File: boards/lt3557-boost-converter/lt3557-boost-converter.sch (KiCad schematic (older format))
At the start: 3 parts

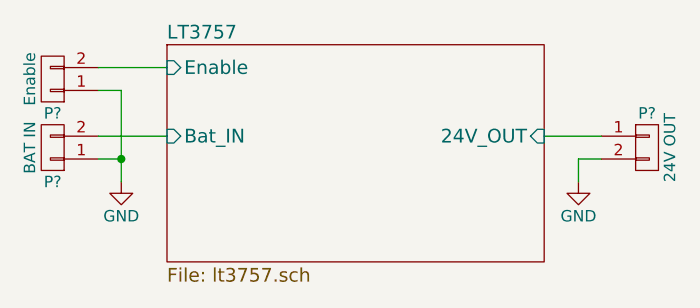
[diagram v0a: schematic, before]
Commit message: lt3557-boost-converter: schematic finished; parts selected; footprints assigned
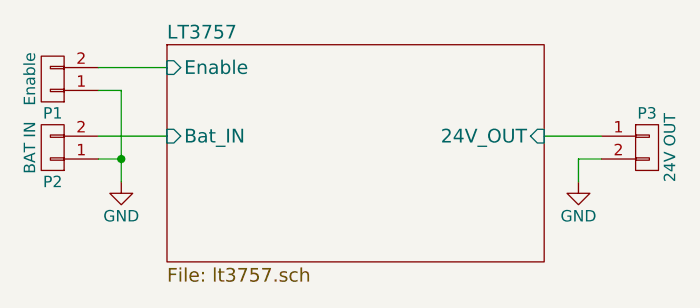
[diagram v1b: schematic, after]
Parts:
- P1: renamed from P?; footprint (none) -> Pin_Headers:Pin_Header_Straight_1x02
- P2, P3: renamed from P?; footprint (none) -> Connect:bornier2
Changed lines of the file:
@@
 $EndDescr
 $Comp
-L CONN_01X02 P?
+L CONN_01X02 P2
 U 1 1 588F8DF1
 P 3950 3750
-F 0 "P?" H 3950 3900 50  0000 C CNN
+F 0 "P2" H 3950 3900 50  0000 C CNN
 F 1 "BAT IN" V 4050 3750 50  0000 C CNN
-F 2 "" H 3950 3750 50  0000 C CNN
+F 2 "Connect:bornier2" H 3950 3750 50  0001 C CNN
 F 3 "" H 3950 3750 50  0000 C CNN
 	1    3950 3750
@@
 $EndComp
 $Comp
-L CONN_01X02 P?
+L CONN_01X02 P3
 U 1 1 588F8E73
 P 6550 3750
-F 0 "P?" H 6550 3900 50  0000 C CNN
+F 0 "P3" H 6550 3900 50  0000 C CNN
 F 1 "24V OUT" V 6650 3750 50  0000 C CNN
-F 2 "" H 6550 3750 50  0000 C CNN
+F 2 "Connect:bornier2" H 6550 3750 50  0001 C CNN
 F 3 "" H 6550 3750 50  0000 C CNN
 	1    6550 3750
@@
 $EndComp
 $Comp
-L GND #PWR?
+L GND #PWR01
 U 1 1 588F8FEC
 P 6250 3900
-F 0 "#PWR?" H 6250 3650 50  0001 C CNN
+F 0 "#PWR01" H 6250 3650 50  0001 C CNN
 F 1 "GND" H 6250 3750 50  0000 C CNN
 F 2 "" H 6250 3900 50  0000 C CNN
@@
 $EndComp
 $Comp
-L GND #PWR?
+L GND #PWR02
 U 1 1 588F9004
 P 4250 3900
-F 0 "#PWR?" H 4250 3650 50  0001 C CNN
+F 0 "#PWR02" H 4250 3650 50  0001 C CNN
 F 1 "GND" H 4250 3750 50  0000 C CNN
 F 2 "" H 4250 3900 50  0000 C CNN
@@
 $EndSheet
 $Comp
-L CONN_01X02 P?
+L CONN_01X02 P1
 U 1 1 588F9182
 P 3950 3450
-F 0 "P?" H 3950 3600 50  0000 C CNN
+F 0 "P1" H 3950 3600 50  0000 C CNN
 F 1 "Enable" V 4050 3450 50  0000 C CNN
-F 2 "" H 3950 3450 50  0000 C CNN
+F 2 "Pin_Headers:Pin_Header_Straight_1x02" H 3950 3450 50  0001 C CNN
 F 3 "" H 3950 3450 50  0000 C CNN
 	1    3950 3450
